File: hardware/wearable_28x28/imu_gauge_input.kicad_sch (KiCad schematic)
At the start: 11 parts, among them U20 BMI270, U21 MAX17048G+T10

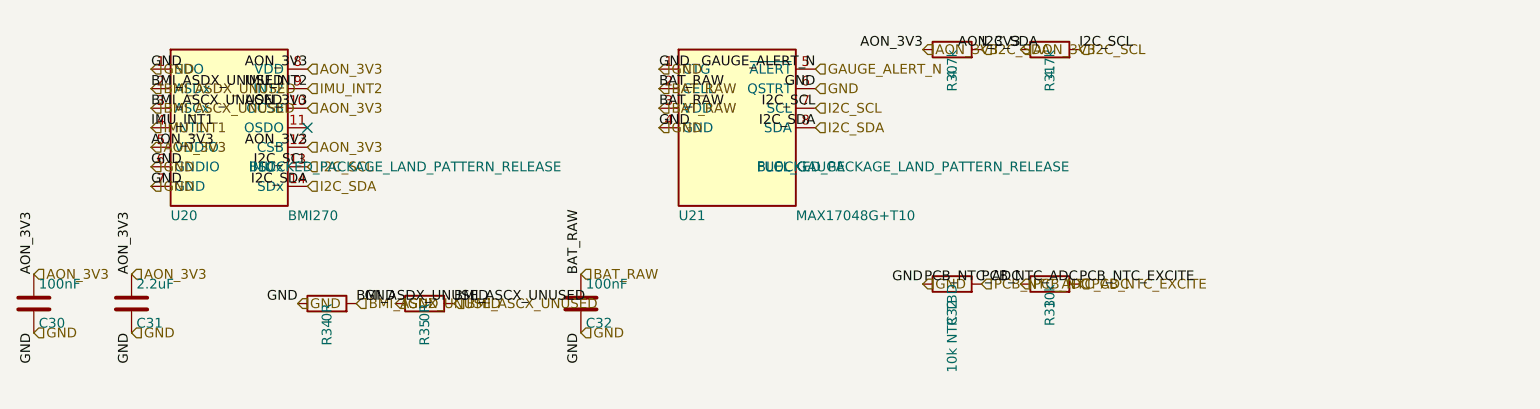
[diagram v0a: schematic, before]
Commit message: Release verified charger and sensor footprints
Co-authored-by: illiapliukhin <illiapliukhin@users.noreply.github.com>
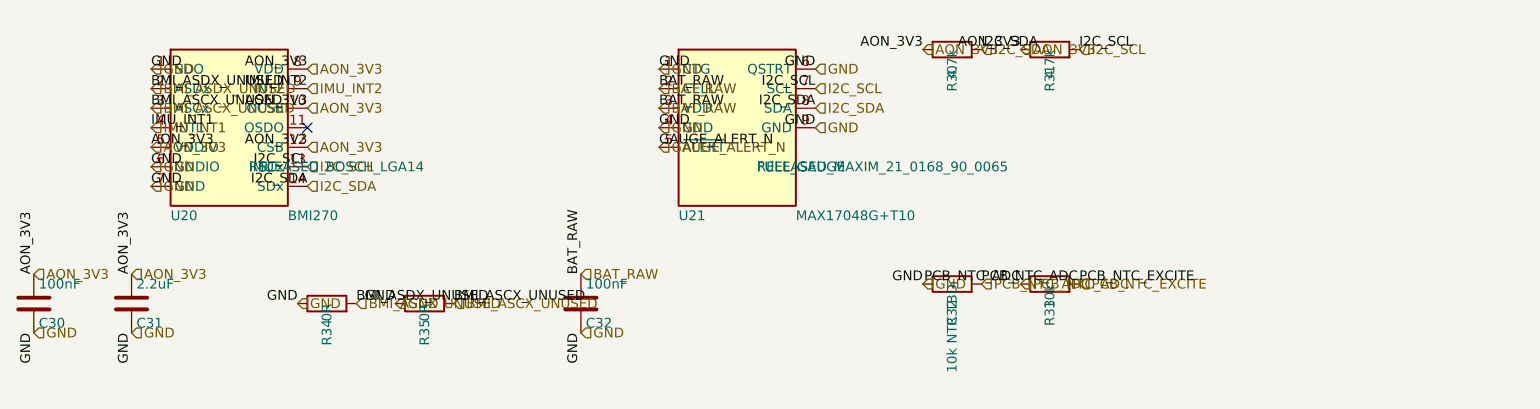
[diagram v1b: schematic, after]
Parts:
- U20: footprint (none) -> Package_LGA:Bosch_LGA-14_3x2.5mm_P0.5mm; FootprintStatus BLOCKED_PACKAGE_LAND_PATTERN_RELEASE -> RELEASED_BOSCH_LGA14
- U21: footprint (none) -> Package_DFN_QFN:TDFN-8-1EP_2x2mm_P0.5mm_EP0.8x1.2mm; FootprintStatus BLOCKED_PACKAGE_LAND_PATTERN_RELEASE -> RELEASED_MAXIM_21_0168_90_0065
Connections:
- net GND: now also U21.9 (GND)
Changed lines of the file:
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@@
 	)
 	(label "GAUGE_ALERT_N"
-		(at 132.08 48.26 180)
-		(effects
-			(font
-				(size 1.27 1.27)
-			)
-			(justify right bottom)
+		(at 111.76 58.42 0)
+		(effects
+			(font
+				(size 1.27 1.27)
+			)
+			(justify left bottom)
 		)
 	)
@@
 	)
 	(label "I2C_SCL"
-		(at 132.08 53.34 180)
+		(at 132.08 50.8 180)
 		(effects
 			(font
@@
 	)
 	(label "GND"
-		(at 132.08 50.8 180)
+		(at 132.08 48.26 180)
 		(effects
 			(font
@@
 		)
 	)
+	(label "GND"
+		(at 132.08 55.88 180)
+		(effects
+			(font
+				(size 1.27 1.27)
+			)
+			(justify right bottom)
+		)
+	)
 	(label "AON_3V3"
 		(at 66.04 58.42 180)
@@
 	)
 	(label "I2C_SDA"
-		(at 132.08 55.88 180)
+		(at 132.08 53.34 180)
 		(effects
 			(font
@@
 		)
 	)
+	(hierarchical_label "GND"
+		(shape input)
+		(at 132.08 55.88 0)
+		(effects
+			(font
+				(size 1.27 1.27)
+			)
+			(justify left)
+		)
+	)
 	(hierarchical_label "AON_3V3"
 		(shape input)
@@
 	(hierarchical_label "I2C_SCL"
 		(shape input)
+		(at 132.08 50.8 0)
+		(effects
+			(font
+				(size 1.27 1.27)
+			)
+			(justify left)
+		)
+	)
+	(hierarchical_label "AON_3V3"
+		(shape input)
+		(at 146.05 45.72 0)
+		(effects
+			(font
+				(size 1.27 1.27)
+			)
+			(justify left)
+		)
+	)
+	(hierarchical_label "PCB_NTC_ADC"
+		(shape input)
+		(at 158.75 76.2 0)
+		(effects
+			(font
+				(size 1.27 1.27)
+			)
+			(justify left)
+		)
+	)
+	(hierarchical_label "BAT_RAW"
+		(shape input)
+		(at 101.6 74.93 0)
+		(effects
+			(font
+				(size 1.27 1.27)
+			)
+			(justify left)
+		)
+	)
+	(hierarchical_label "GND"
+		(shape input)
+		(at 77.47 78.74 0)
+		(effects
+			(font
+				(size 1.27 1.27)
+			)
+			(justify left)
+		)
+	)
+	(hierarchical_label "I2C_SDA"
+		(shape input)
 		(at 132.08 53.34 0)
 		(effects
@@
 	(hierarchical_label "AON_3V3"
 		(shape input)
-		(at 146.05 45.72 0)
-		(effects
-			(font
-				(size 1.27 1.27)
-			)
-			(justify left)
-		)
-	)
-	(hierarchical_label "PCB_NTC_ADC"
-		(shape input)
-		(at 158.75 76.2 0)
+		(at 30.48 74.93 0)
+		(effects
+			(font
+				(size 1.27 1.27)
+			)
+			(justify left)
+		)
+	)
+	(hierarchical_label "AON_3V3"
+		(shape input)
+		(at 66.04 53.34 0)
+		(effects
+			(font
+				(size 1.27 1.27)
+			)
+			(justify left)
+		)
+	)
+	(hierarchical_label "GND"
+		(shape input)
+		(at 45.72 60.96 0)
 		(effects
 			(font
@@
 	(hierarchical_label "BAT_RAW"
 		(shape input)
-		(at 101.6 74.93 0)
-		(effects
-			(font
-				(size 1.27 1.27)
-			)
-			(justify left)
-		)
-	)
-	(hierarchical_label "GND"
-		(shape input)
-		(at 77.47 78.74 0)
-		(effects
-			(font
-				(size 1.27 1.27)
-			)
-			(justify left)
-		)
-	)
-	(hierarchical_label "I2C_SDA"
-		(shape input)
-		(at 132.08 55.88 0)
-		(effects
-			(font
-				(size 1.27 1.27)
-			)
-			(justify left)
-		)
-	)
-	(hierarchical_label "AON_3V3"
-		(shape input)
-		(at 30.48 74.93 0)
-		(effects
-			(font
-				(size 1.27 1.27)
-			)
-			(justify left)
-		)
-	)
-	(hierarchical_label "AON_3V3"
-		(shape input)
-		(at 66.04 53.34 0)
-		(effects
-			(font
-				(size 1.27 1.27)
-			)
-			(justify left)
-		)
-	)
-	(hierarchical_label "GND"
-		(shape input)
-		(at 45.72 60.96 0)
-		(effects
-			(font
-				(size 1.27 1.27)
-			)
-			(justify left)
-		)
-	)
-	(hierarchical_label "BAT_RAW"
-		(shape input)
 		(at 111.76 50.8 0)
 		(effects
@@
 	(hierarchical_label "GND"
 		(shape input)
-		(at 132.08 50.8 0)
+		(at 132.08 48.26 0)
 		(effects
 			(font
@@
 	(hierarchical_label "GAUGE_ALERT_N"
 		(shape input)
-		(at 132.08 48.26 0)
+		(at 111.76 58.42 0)
 		(effects
 			(font
@@
 			)
 		)
-		(property "Footprint" ""
+		(property "Footprint" "Package_LGA:Bosch_LGA-14_3x2.5mm_P0.5mm"
 			(at 55.88 55.88 0)
 			(hide yes)
@@
 			)
 		)
-		(property "FootprintStatus" "BLOCKED_PACKAGE_LAND_PATTERN_RELEASE"
+		(property "FootprintStatus" "RELEASED_BOSCH_LGA14"
 			(at 58.42 60.9599 0)
 			(show_name no)
@@
 			)
 		)
-		(property "Footprint" ""
+		(property "Footprint" "Package_DFN_QFN:TDFN-8-1EP_2x2mm_P0.5mm_EP0.8x1.2mm"
 			(at 121.92 55.88 0)
 			(hide yes)
@@
 			)
 		)
-		(property "FootprintStatus" "BLOCKED_PACKAGE_LAND_PATTERN_RELEASE"
+		(property "FootprintStatus" "RELEASED_MAXIM_21_0168_90_0065"
 			(at 124.46 60.9599 0)
 			(show_name no)
@@
 		(pin "8"
 		)
+		(pin "9"
+		)
 		(instances

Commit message: Regenerate hierarchies with selected EVT parts
Co-authored-by: illiapliukhin <illiapliukhin@users.noreply.github.com>
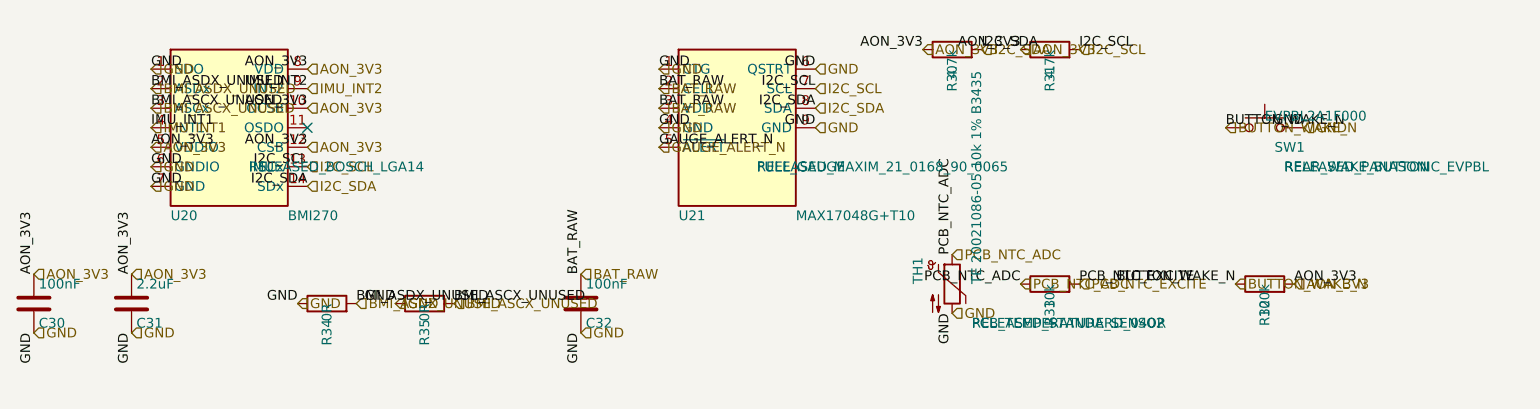
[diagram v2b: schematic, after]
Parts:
- added SW1: EVPBL2A1F000, PartSignal_Packages:Panasonic_EVPBL2A1F000_Switch, symbol Switch:SW_Push
- added TH1: TE 20021086-05 10k 1% B3435, Resistor_SMD:R_0402_1005Metric, symbol Device:Thermistor_NTC
- R32: value 10k NTC TBD -> 100k
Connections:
- net AON_3V3: now also R32.2
- net GND: now also SW1.2, TH1.2; no longer R32.1
- net PCB_NTC_ADC: now also TH1.1; no longer R32.2
- new net BUTTON_WAKE_N: R32.1, SW1.1
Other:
- moved on the sheet: R32
